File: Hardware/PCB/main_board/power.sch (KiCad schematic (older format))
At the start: 14 parts, among them J21 GND, J22 GND, J23 +5V, J24 +5VA, J4 USB_B, J7 GND, J8 GND

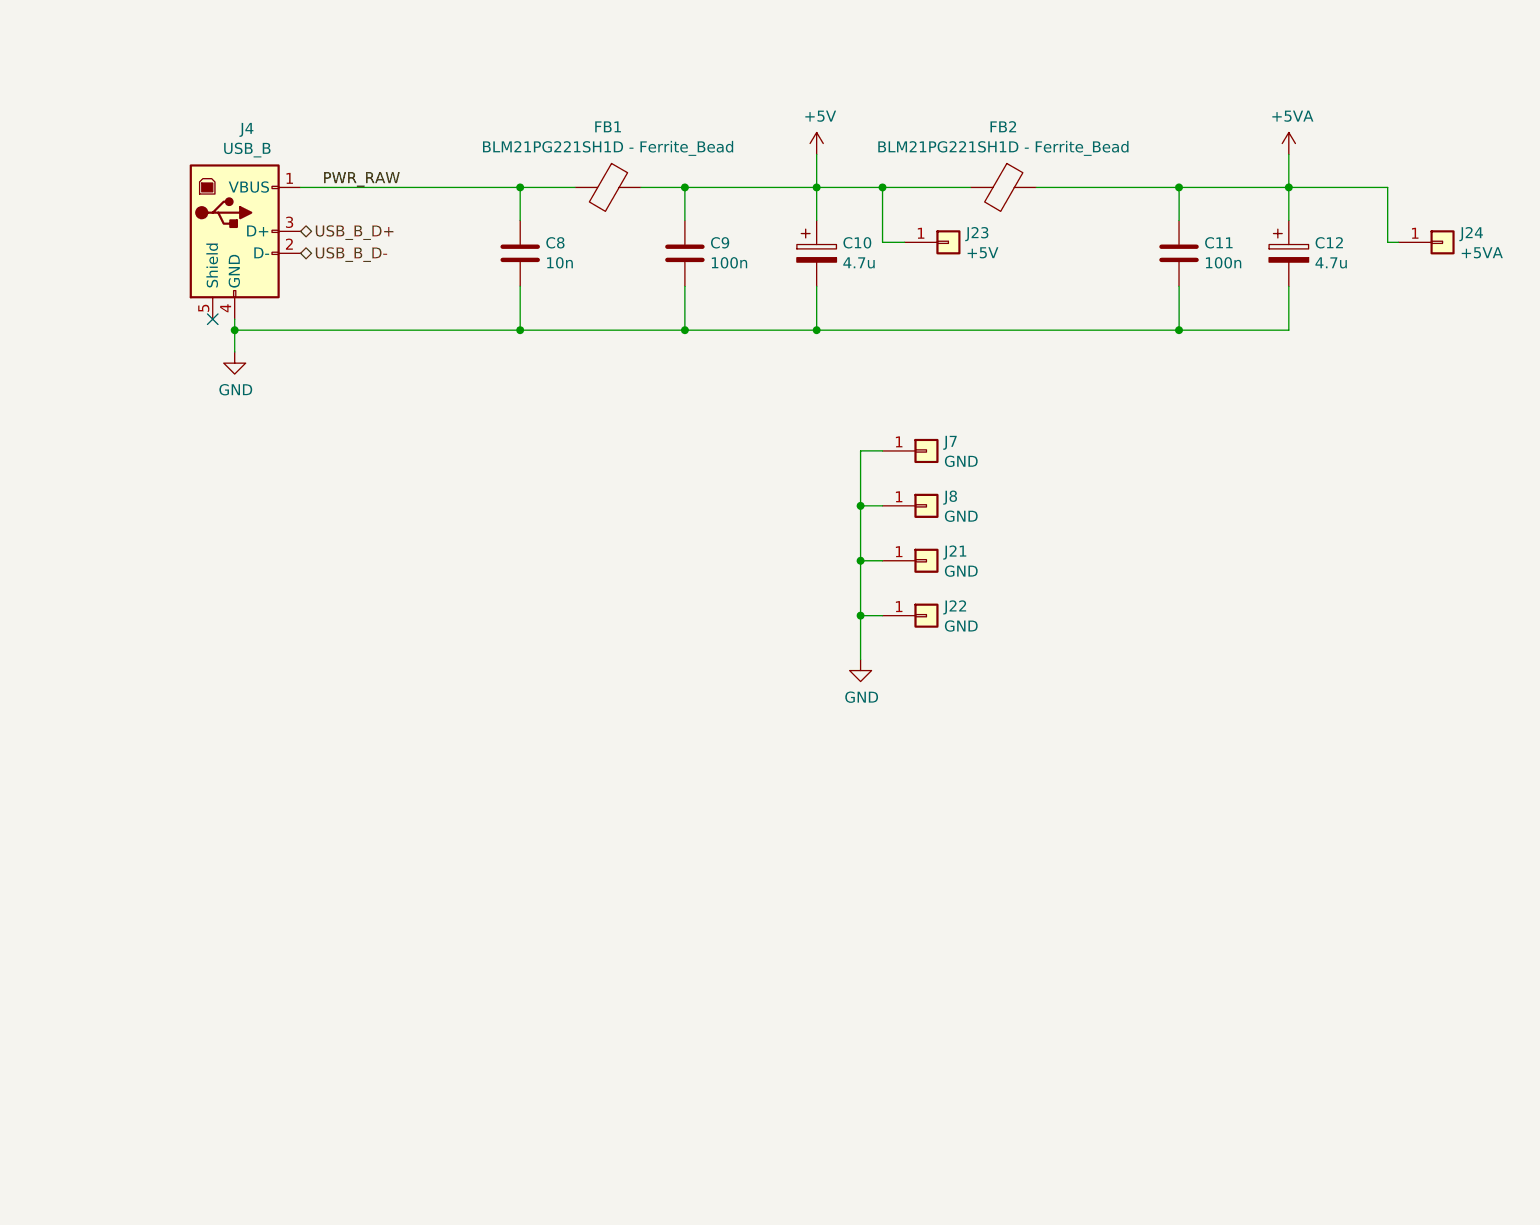
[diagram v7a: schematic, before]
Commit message: Use bare STM32 instead of nucleo board. Schematics update
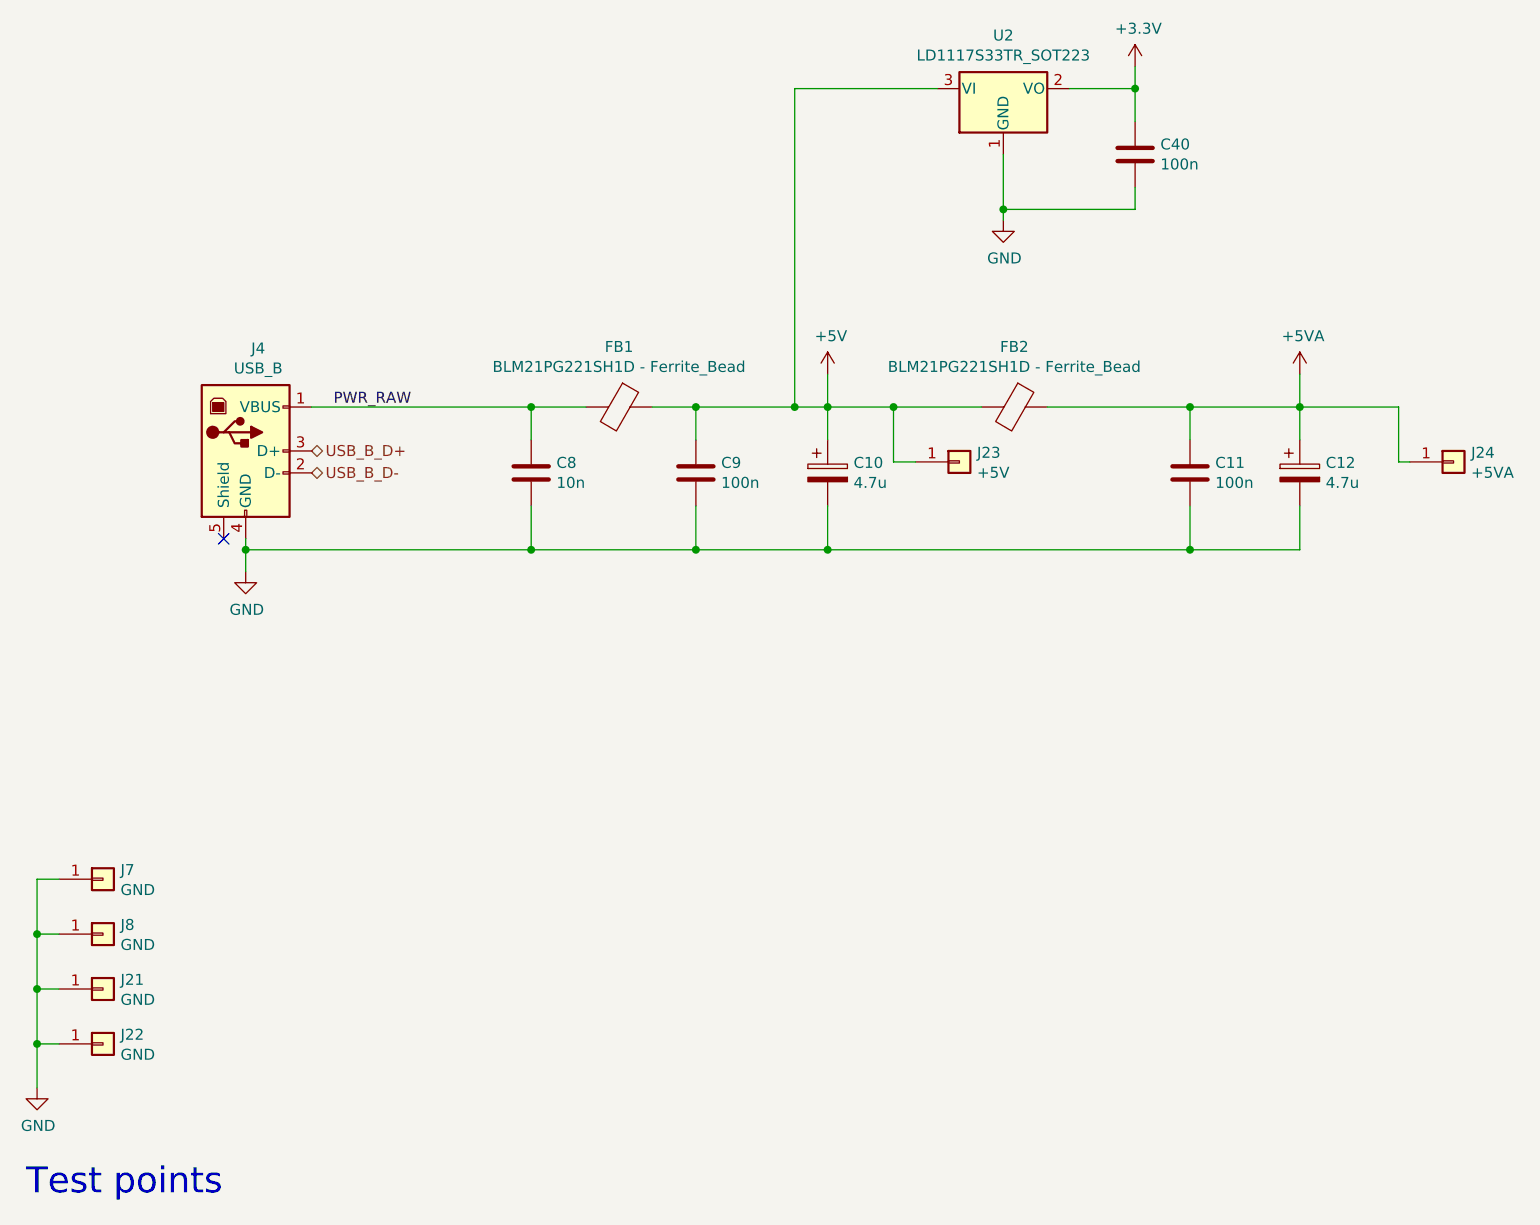
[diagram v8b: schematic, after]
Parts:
- added C40: 100n, Capacitor_SMD:C_0805_2012Metric, symbol Device:C
- added U2: LD1117S33TR_SOT223, Package_TO_SOT_SMD:SOT-223-3_TabPin2, symbol Regulator_Linear:LD1117S33TR_SOT223
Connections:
- net +5V: now also U2.3 (VI)
- net GND: now also C40.2, U2.1 (GND)
- new net +3V3: C40.1, U2.2 (VO)
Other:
- note added: "Test points"
- moved on the sheet: C10, C11, C12, C8, C9, FB1, FB2, J21, J22, J23, J24, J4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
